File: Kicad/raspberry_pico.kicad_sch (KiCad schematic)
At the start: 9 parts, among them Q201 DMG2305UX, U201 Pico

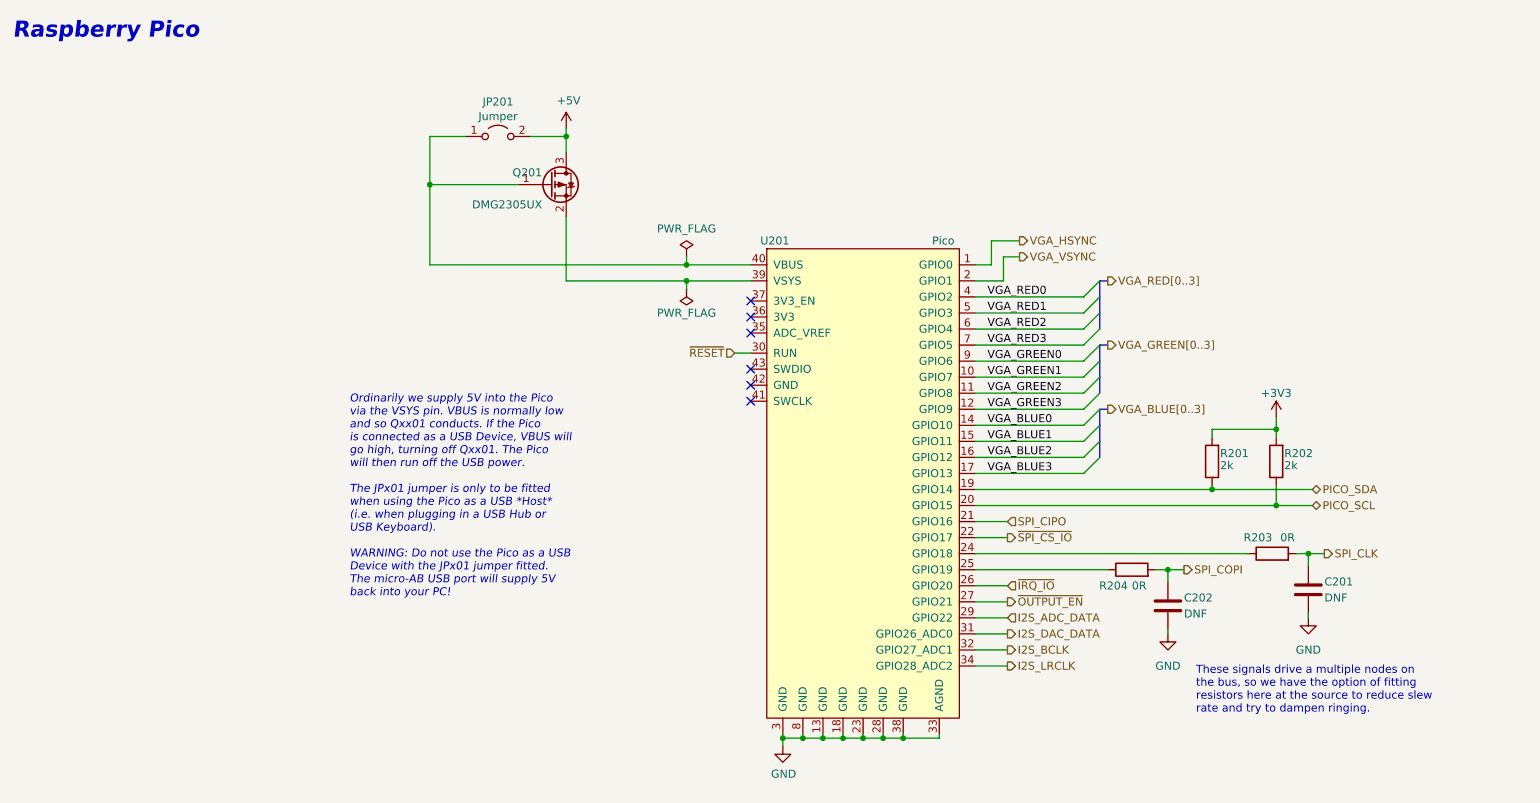
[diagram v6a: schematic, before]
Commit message: Updated to Kicad 8.0.3.
Had to disable PCB/Library footprint mismatch, and schematic grid alignment errors (I was on 25mil, Kicad really wants to use 50mil).
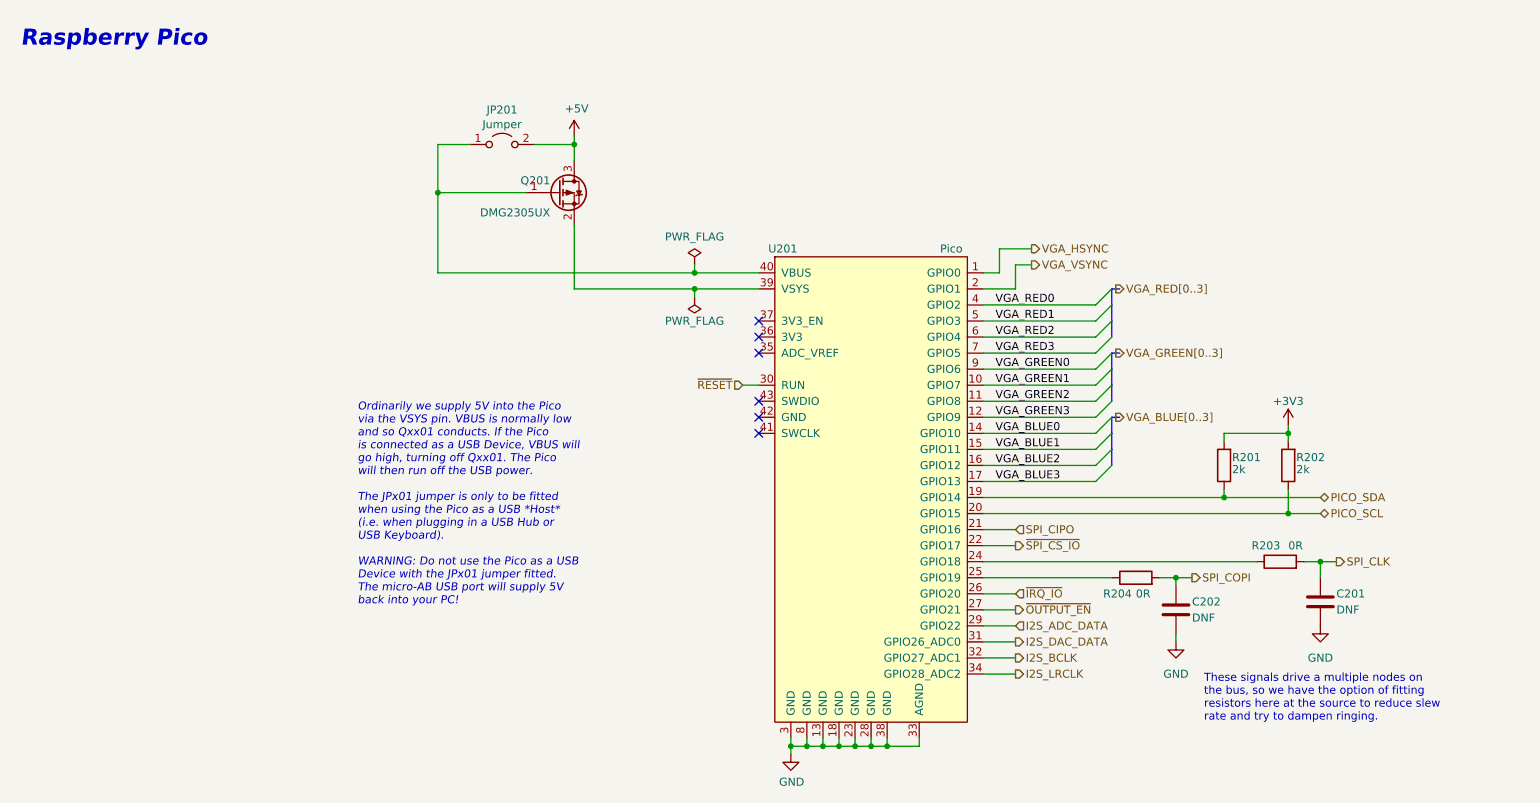
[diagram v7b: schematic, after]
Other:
- moved on the sheet: C201, C202, JP201, Q201, R201, R202, R203, R204, U201
